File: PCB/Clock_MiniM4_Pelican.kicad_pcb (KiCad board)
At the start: 2 copper layers, 152.4 x 33 mm, 9 parts, among them J1 5V_POWER_INPUT, M1 Feather_M4_Express, M2 DS3231_RTC_FeatherWing_3028, M3 4-Bit_Level_Converter_757, U1 1.2-inch_7-segment_LED_HT16K3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

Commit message: update PCB design
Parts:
- moved M2 1.27 mm to (177.8, 52.1)
- moved M3 0.83 mm to (141.0, 48.3)
- moved BZ1 0.64 mm to (138.4, 59.7)
- moved S1 0.64 mm to (208.9, 52.1)
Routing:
- net /SDA: track 76.7 -> 90.4 mm, vias 0 -> 1
- net /SCL: track 81.9 -> 89.2 mm
- net +3V3: track 111.3 -> 104.9 mm
- net /USB: track 151.4 -> 156.9 mm
- net /D5: track 132.7 -> 138.1 mm
- net /D6: track 136.3 -> 139.9 mm
- net /D9: track 106.8 -> 108.2 mm
- net /5V_SDA: track 30.5 -> 29.7 mm
- net /5V_SCL: track 36.1 -> 35.3 mm
- net GND: vias 6 -> 7

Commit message: initial repo load
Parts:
- added J**: 2.1mm_THT_DC_panel_power_conn_610, Adafruit:2.1mm_THT_DC_panel_power_conn_610, F.Cu at (220.5, 91.0)

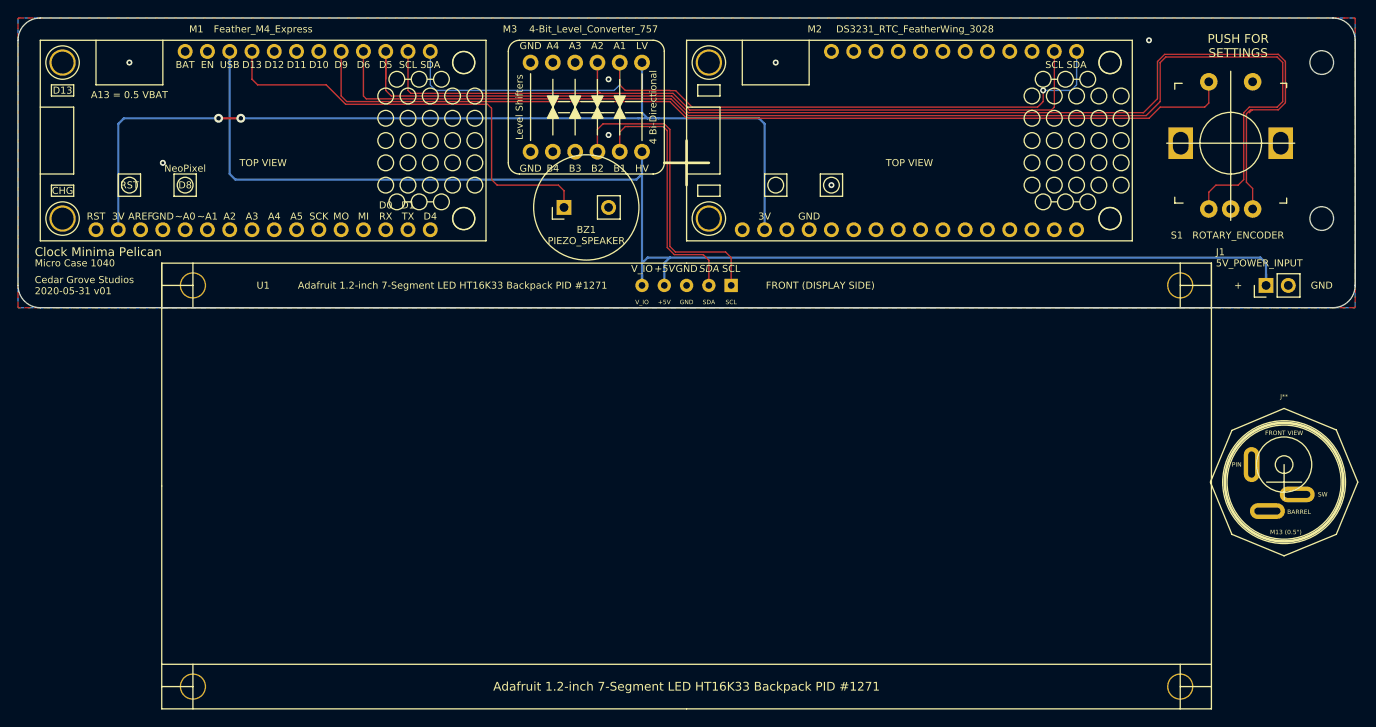
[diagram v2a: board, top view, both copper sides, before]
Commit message: update PCB; display bright in param file
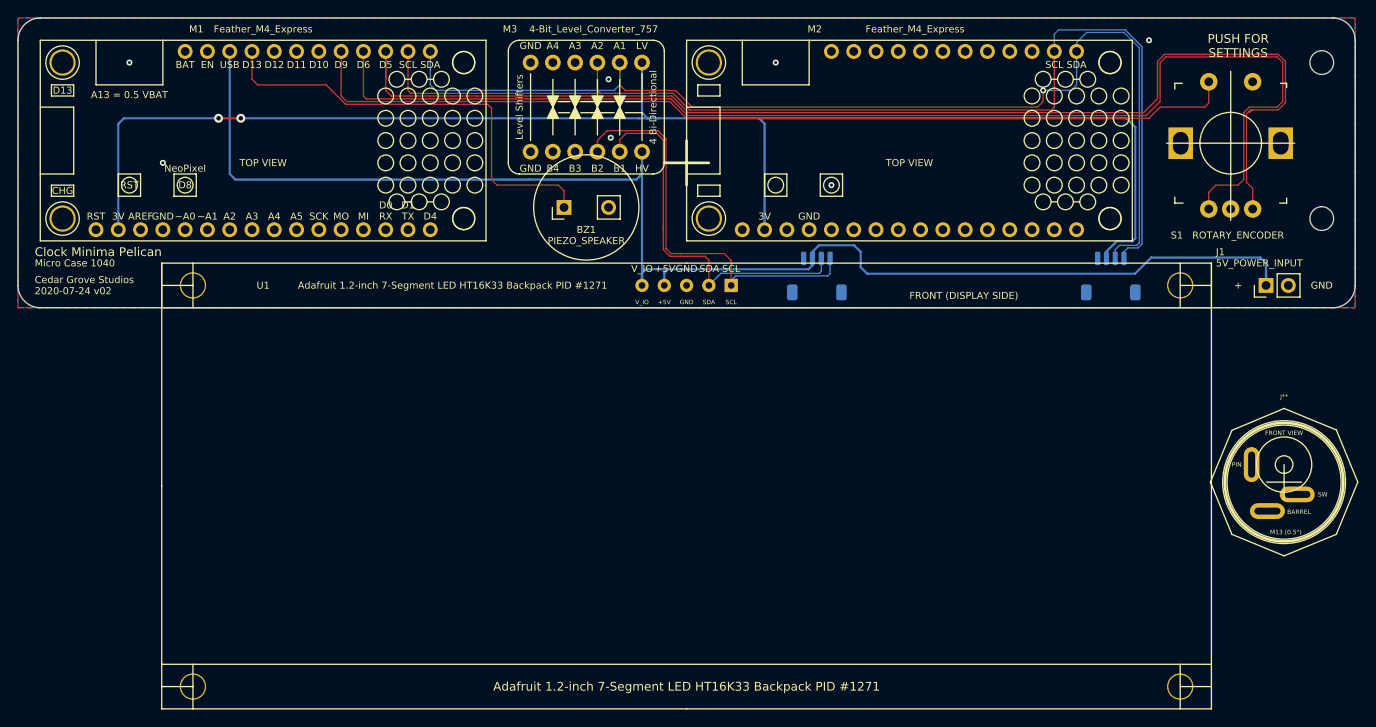
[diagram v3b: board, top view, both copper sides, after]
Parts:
- added J2: STEMMA-QT_3V, Connector_JST:JST_SH_SM04B-SRSS-TB_1x04-1MP_P1.00mm_Horizontal, B.Cu at (200.8, 67.5)
- added J3: STEMMA-QT_5V, Connector_JST:JST_SH_SM04B-SRSS-TB_1x04-1MP_P1.00mm_Horizontal, B.Cu at (167.2, 67.5)
- M2: value DS3231_RTC_FeatherWing_3028 -> Feather_M4_Express
- U1: value 1.2-inch_7-segment_LED_HT16K33_backpack_1271 -> 1.2-inch_7-segment_LED_HT16K33_backpack
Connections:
- M1 pad 1: (no net) -> Net-(M1-Pad1)
- M1 pad 10: (no net) -> Net-(M1-Pad10)
- M1 pad 11: (no net) -> Net-(M1-Pad11)
- M1 pad 12: (no net) -> Net-(M1-Pad12)
- M1 pad 13: (no net) -> Net-(M1-Pad13)
- M1 pad 14: (no net) -> Net-(M1-Pad14)
- M1 pad 15: (no net) -> Net-(M1-Pad15)
- M1 pad 16: (no net) -> Net-(M1-Pad16)
- M1 pad 17: (no net) -> Net-(M1-Pad17)
- M1 pad 18: (no net) -> Net-(M1-Pad18)
- M1 pad 21: (no net) -> Net-(M1-Pad21)
- M1 pad 22: (no net) -> Net-(M1-Pad22)
- M1 pad 23: (no net) -> Net-(M1-Pad23)
- M1 pad 3: (no net) -> Net-(M1-Pad3)
- M1 pad 5: (no net) -> Net-(M1-Pad5)
- M1 pad 6: (no net) -> Net-(M1-Pad6)
- M1 pad 7: (no net) -> Net-(M1-Pad7)
- M1 pad 8: (no net) -> Net-(M1-Pad8)
- M1 pad 9: (no net) -> Net-(M1-Pad9)
- M2 pad 1: (no net) -> Net-(M2-Pad1)
- M2 pad 10: (no net) -> Net-(M2-Pad10)
- M2 pad 11: (no net) -> Net-(M2-Pad11)
- M2 pad 12: (no net) -> Net-(M2-Pad12)
- M2 pad 13: (no net) -> Net-(M2-Pad13)
- M2 pad 14: (no net) -> Net-(M2-Pad14)
- M2 pad 15: (no net) -> Net-(M2-Pad15)
- M2 pad 16: (no net) -> Net-(M2-Pad16)
- M2 pad 17: (no net) -> Net-(M2-Pad17)
- M2 pad 18: (no net) -> Net-(M2-Pad18)
- M2 pad 19: (no net) -> Net-(M2-Pad19)
- M2 pad 20: (no net) -> Net-(M2-Pad20)
- M2 pad 21: (no net) -> Net-(M2-Pad21)
- M2 pad 22: (no net) -> Net-(M2-Pad22)
- M2 pad 23: (no net) -> Net-(M2-Pad23)
- M2 pad 24: (no net) -> Net-(M2-Pad24)
- M2 pad 25: (no net) -> Net-(M2-Pad25)
- M2 pad 26: (no net) -> Net-(M2-Pad26)
- M2 pad 3: (no net) -> Net-(M2-Pad3)
- M2 pad 5: (no net) -> Net-(M2-Pad5)
- M2 pad 6: (no net) -> Net-(M2-Pad6)
- M2 pad 7: (no net) -> Net-(M2-Pad7)
- M2 pad 8: (no net) -> Net-(M2-Pad8)
- M2 pad 9: (no net) -> Net-(M2-Pad9)
- M3 pad 4: (no net) -> Net-(M3-Pad4)
- M3 pad 5: (no net) -> Net-(M3-Pad5)
- M3 pad 8: (no net) -> Net-(M3-Pad8)
- M3 pad 9: (no net) -> Net-(M3-Pad9)
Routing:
- net +3V3: track 104.9 -> 165.6 mm
- net /SCL: track 89.2 -> 127.8 mm
- net /SDA: track 90.4 -> 126.0 mm
- net /5V_SDA: track 29.7 -> 43.5 mm
- net /5V_SCL: track 35.3 -> 47.3 mm
- net /USB: track 156.9 -> 160.5 mm
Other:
- board text added: "2020-07-24 v02"
- board text removed: "2020-05-31 v01"

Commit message: Update new PCB design - fix STEMMA-QT pinout
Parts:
- moved M1 0.07 mm to (104.2, 52.1)
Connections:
- J2 pad 1: /SCL -> GND
- J2 pad 2: /SDA -> +3V3
- J2 pad 3: +3V3 -> /SDA
- J2 pad 4: GND -> /SCL
- J3 pad 1: /5V_SCL -> GND
- J3 pad 2: /5V_SDA -> /USB
- J3 pad 3: /USB -> /5V_SDA
- J3 pad 4: GND -> /5V_SCL
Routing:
- net +3V3: track 165.6 -> 152.5 mm
- net /SCL: track 127.8 -> 120.0 mm, vias 0 -> 1
- net /SDA: track 126.0 -> 119.7 mm
- net /5V_SCL: track 47.3 -> 42.3 mm, vias 0 -> 1
- net /USB: track 160.5 -> 162.6 mm
- net /5V_SDA: track 43.5 -> 45.1 mm
- net GND: track 0.00 -> 0.75 mm

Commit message: update pcb
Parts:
- added G***: LOGO, Adafruit:CG_logo_25-4mm, B.Cu at (92.8, 53.1)
- added G***: Binka, Adafruit:Blinka, B.Cu at (82.9, 53.3)
- added G***: STEMMA-QT_LOGO, Adafruit:New_STEMMA-QT_logo, B.Cu at (176.0, 65.9)
- added G***: STEMMA-QT_LOGO, Adafruit:New_STEMMA-QT_logo, B.Cu at (192.2, 66.0)
- M2: value Feather_M4_Express -> DS3231_RTC_FeatherWing
- M3: value 4-Bit_Level_Converter_757 -> 4-Bit_Level_Converter
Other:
- board text added: "2020-08-05 v02"
- board text added: "3V HOST"
- board text added: "5V HOST"
- board text removed: "2020-07-24 v02"
